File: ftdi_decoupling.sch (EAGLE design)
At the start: 10 parts, among them J1 FTDI_DEVICE, U1 ATMEGA328P_TQFP

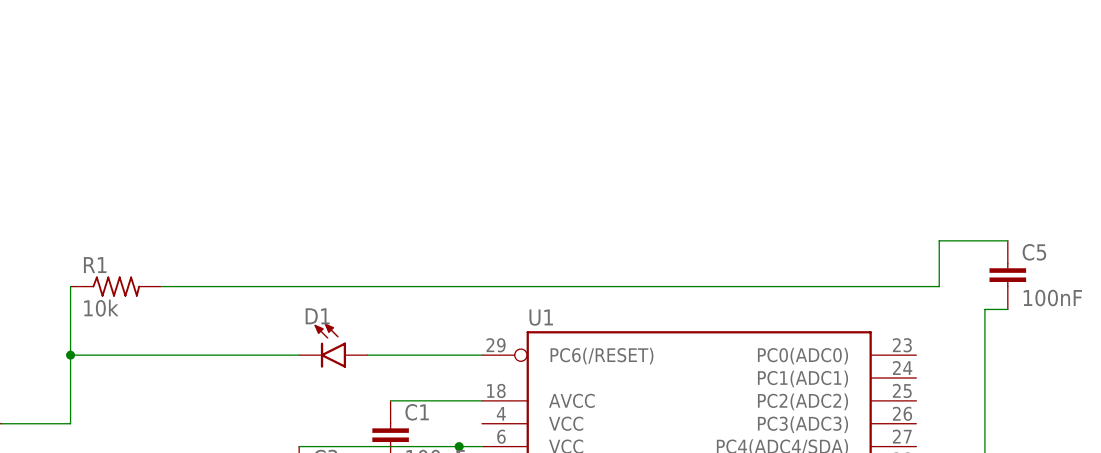
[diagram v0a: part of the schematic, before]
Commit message: Updated schematic. TODO: voltage divider, voltage regulator, motor driver, battery
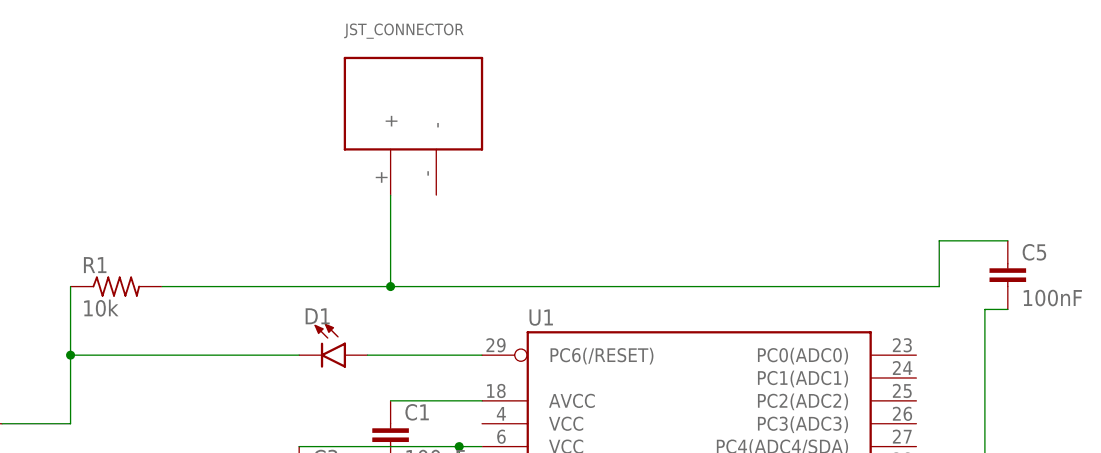
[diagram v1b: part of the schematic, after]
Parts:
- added U$1: JST_CONNECTOR_FEMALE, quad:JST_CONNECTOR_FEMALE
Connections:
- net N$11: now also U$1.+
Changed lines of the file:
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@@
 <part name="D1" library="SparkFun-LED" deviceset="LED" device="0603"/>
 <part name="S2" library="switch" library_urn="urn:adsk.eagle:library:380" deviceset="55?" device="01" package3d_urn="urn:adsk.eagle:package:27750/1"/>
+<part name="U$1" library="quad" deviceset="JST_CONNECTOR_FEMALE" device=""/>
 </parts>
 <sheets>
@@
 <instance part="D1" gate="G$1" x="22.86" y="68.58" rot="R270"/>
 <instance part="S2" gate="G$1" x="-20.32" y="58.42"/>
+<instance part="U$1" gate="G$1" x="30.48" y="96.52"/>
 </instances>
 <busses>
@@
 <wire x1="88.9" y1="81.28" x2="88.9" y2="76.2" width="0.1524" layer="91"/>
 <pinref part="R1" gate="G$1" pin="2"/>
-<wire x1="88.9" y1="76.2" x2="2.54" y2="76.2" width="0.1524" layer="91"/>
+<wire x1="88.9" y1="76.2" x2="27.94" y2="76.2" width="0.1524" layer="91"/>
+<pinref part="U$1" gate="G$1" pin="+"/>
+<wire x1="27.94" y1="76.2" x2="2.54" y2="76.2" width="0.1524" layer="91"/>
+<wire x1="27.94" y1="86.36" x2="27.94" y2="76.2" width="0.1524" layer="91"/>
+<junction x="27.94" y="76.2"/>
 </segment>
 </net>
